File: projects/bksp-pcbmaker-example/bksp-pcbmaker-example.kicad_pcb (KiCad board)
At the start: 2 copper layers, 100 x 100 mm, 2 parts

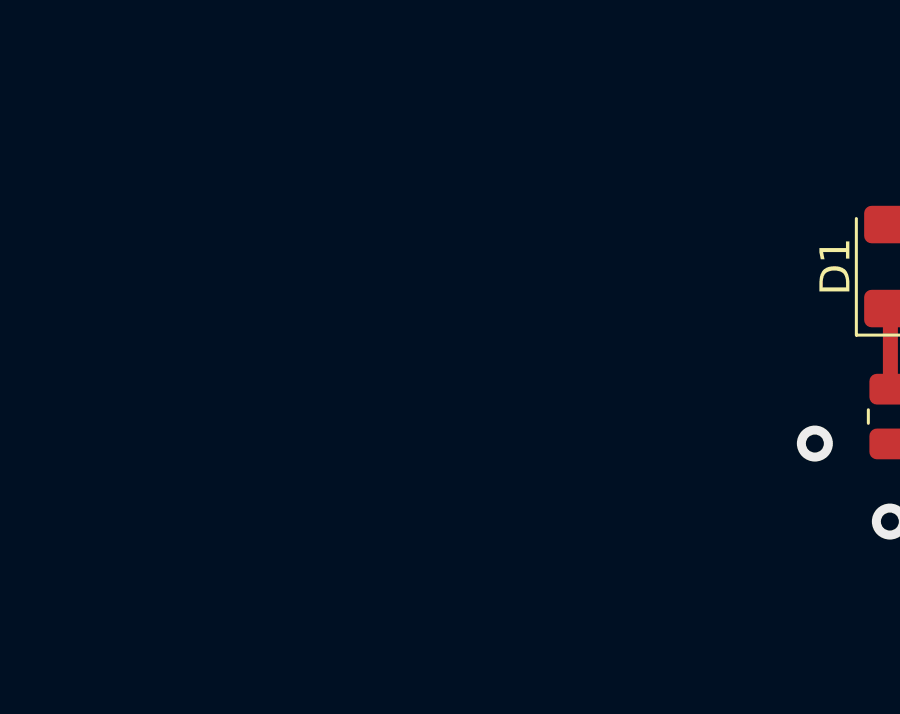
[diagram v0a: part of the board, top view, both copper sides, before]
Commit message: feat(reference): update DRC & Copper Fill settings in a reference project
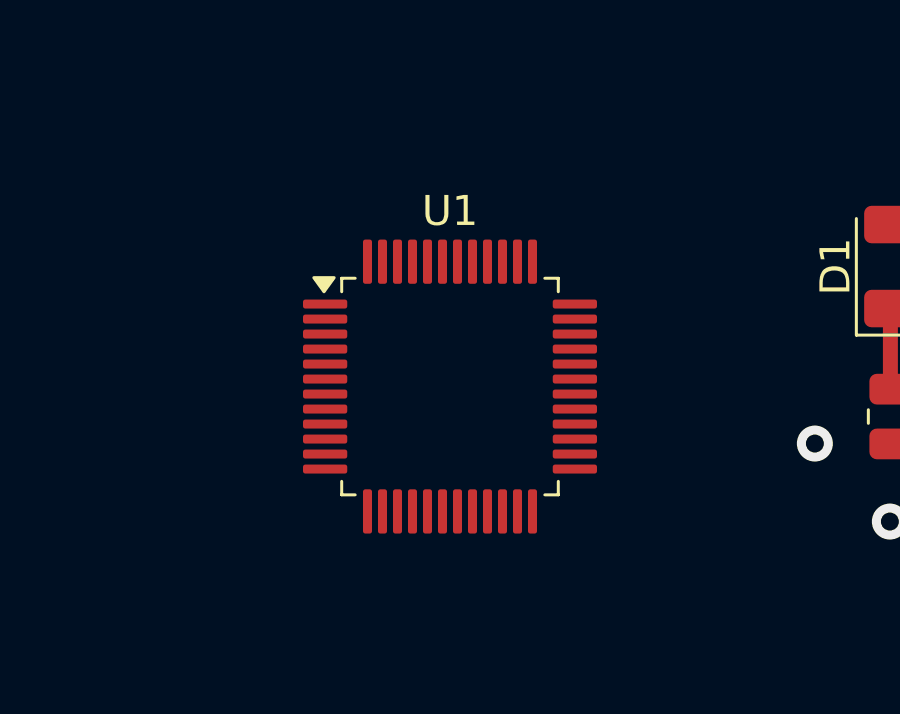
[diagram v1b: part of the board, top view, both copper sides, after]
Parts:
- added U1: CH32L103C8T6, Package_QFP:LQFP-48_7x7mm_P0.5mm, F.Cu at (135.0, 100.0)
